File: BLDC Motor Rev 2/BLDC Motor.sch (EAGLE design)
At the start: 51 parts, among them IC1 7805TV, IC2 7815TV, Q1 TP2104, Q10 TP2104, Q12 IRFS, Q13 TP2104, Q15 IRFS, Q16 TP2104, Q18 IRFS, Q3 IRFS, Q4 TP2104, Q6 IRFS, Q7 TP2104, Q9 IRFS, U1 ATMEGA328P_TQFP, Y1 16M

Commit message: Updated BLDC schematic
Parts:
- added R15: 100k, SparkFun:RESISTOR0805-RES
- added R16: 20k, SparkFun:RESISTOR0805-RES
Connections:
- removed net N$12: U1.ADC7
- new net BATTLEVEL: R15.1, R16.2, U1.ADC7
- net BATTPOS: now also R15.2
- net GND: now also R16.1
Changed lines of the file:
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@@
 <grid distance="0.1" unitdist="inch" unit="inch" style="lines" multiple="1" display="no" altdistance="0.01" altunitdist="inch" altunit="inch"/>
 <layers>
-<layer number="1" name="Top" color="4" fill="1" visible="yes" active="no"/>
-<layer number="16" name="Bottom" color="1" fill="1" visible="yes" active="no"/>
-<layer number="17" name="Pads" color="2" fill="1" visible="yes" active="no"/>
-<layer number="18" name="Vias" color="2" fill="1" visible="yes" active="no"/>
-<layer number="19" name="Unrouted" color="6" fill="1" visible="yes" active="no"/>
-<layer number="20" name="Dimension" color="15" fill="1" visible="yes" active="no"/>
-<layer number="21" name="tPlace" color="7" fill="1" visible="yes" active="no"/>
-<layer number="22" name="bPlace" color="7" fill="1" visible="yes" active="no"/>
-<layer number="23" name="tOrigins" color="15" fill="1" visible="yes" active="no"/>
-<layer number="24" name="bOrigins" color="15" fill="1" visible="yes" active="no"/>
-<layer number="25" name="tNames" color="7" fill="1" visible="yes" active="no"/>
-<layer number="26" name="bNames" color="7" fill="1" visible="yes" active="no"/>
-<layer number="27" name="tValues" color="7" fill="1" visible="yes" active="no"/>
-<layer number="28" name="bValues" color="7" fill="1" visible="yes" active="no"/>
+<layer number="1" name="Top" color="4" fill="1" visible="no" active="no"/>
+<layer number="16" name="Bottom" color="1" fill="1" visible="no" active="no"/>
+<layer number="17" name="Pads" color="2" fill="1" visible="no" active="no"/>
+<layer number="18" name="Vias" color="2" fill="1" visible="no" active="no"/>
+<layer number="19" name="Unrouted" color="6" fill="1" visible="no" active="no"/>
+<layer number="20" name="Dimension" color="15" fill="1" visible="no" active="no"/>
+<layer number="21" name="tPlace" color="7" fill="1" visible="no" active="no"/>
+<layer number="22" name="bPlace" color="7" fill="1" visible="no" active="no"/>
+<layer number="23" name="tOrigins" color="15" fill="1" visible="no" active="no"/>
+<layer number="24" name="bOrigins" color="15" fill="1" visible="no" active="no"/>
+<layer number="25" name="tNames" color="7" fill="1" visible="no" active="no"/>
+<layer number="26" name="bNames" color="7" fill="1" visible="no" active="no"/>
+<layer number="27" name="tValues" color="7" fill="1" visible="no" active="no"/>
+<layer number="28" name="bValues" color="7" fill="1" visible="no" active="no"/>
 <layer number="29" name="tStop" color="7" fill="3" visible="no" active="no"/>
 <layer number="30" name="bStop" color="7" fill="6" visible="no" active="no"/>
@@
 <layer number="35" name="tGlue" color="7" fill="4" visible="no" active="no"/>
 <layer number="36" name="bGlue" color="7" fill="5" visible="no" active="no"/>
-<layer number="37" name="tTest" color="7" fill="1" visible="yes" active="no"/>
-<layer number="38" name="bTest" color="7" fill="1" visible="yes" active="no"/>
+<layer number="37" name="tTest" color="7" fill="1" visible="no" active="no"/>
+<layer number="38" name="bTest" color="7" fill="1" visible="no" active="no"/>
 <layer number="39" name="tKeepout" color="4" fill="11" visible="no" active="no"/>
 <layer number="40" name="bKeepout" color="1" fill="11" visible="no" active="no"/>
@@
 <layer number="44" name="Drills" color="7" fill="1" visible="no" active="no"/>
 <layer number="45" name="Holes" color="7" fill="1" visible="no" active="no"/>
-<layer number="46" name="Milling" color="3" fill="1" visible="yes" active="no"/>
-<layer number="47" name="Measures" color="7" fill="1" visible="yes" active="no"/>
-<layer number="48" name="Document" color="7" fill="1" visible="yes" active="no"/>
-<layer number="49" name="Reference" color="7" fill="1" visible="yes" active="no"/>
-<layer number="50" name="dxf" color="7" fill="1" visible="yes" active="no"/>
-<layer number="51" name="tDocu" color="7" fill="1" visible="yes" active="no"/>
-<layer number="52" name="bDocu" color="7" fill="1" visible="yes" active="no"/>
-<layer number="53" name="tGND_GNDA" color="7" fill="9" visible="yes" active="no"/>
-<layer number="54" name="bGND_GNDA" color="1" fill="9" visible="yes" active="no"/>
-<layer number="56" name="wert" color="7" fill="1" visible="yes" active="no"/>
-<layer number="57" name="tCAD" color="7" fill="1" visible="yes" active="no"/>
-<layer number="59" name="tCarbon" color="7" fill="1" visible="yes" active="no"/>
-<layer number="60" name="bCarbon" color="7" fill="1" visible="yes" active="no"/>
+<layer number="46" name="Milling" color="3" fill="1" visible="no" active="no"/>
+<layer number="47" name="Measures" color="7" fill="1" visible="no" active="no"/>
+<layer number="48" name="Document" color="7" fill="1" visible="no" active="no"/>
+<layer number="49" name="Reference" color="7" fill="1" visible="no" active="no"/>
+<layer number="50" name="dxf" color="7" fill="1" visible="no" active="no"/>
+<layer number="51" name="tDocu" color="7" fill="1" visible="no" active="no"/>
+<layer number="52" name="bDocu" color="7" fill="1" visible="no" active="no"/>
+<layer number="53" name="tGND_GNDA" color="7" fill="9" visible="no" active="no"/>
+<layer number="54" name="bGND_GNDA" color="1" fill="9" visible="no" active="no"/>
+<layer number="56" name="wert" color="7" fill="1" visible="no" active="no"/>
+<layer number="57" name="tCAD" color="7" fill="1" visible="no" active="no"/>
+<layer number="59" name="tCarbon" color="7" fill="1" visible="no" active="no"/>
+<layer number="60" name="bCarbon" color="7" fill="1" visible="no" active="no"/>
 <layer number="90" name="Modules" color="5" fill="1" visible="yes" active="yes"/>
 <layer number="91" name="Nets" color="2" fill="1" visible="yes" active="yes"/>
@@
 <part name="Q15" library="D2PAK-7" deviceset="NMOSFET-D2PAK-7" device="" value="IRFS"/>
 <part name="Q18" library="D2PAK-7" deviceset="NMOSFET-D2PAK-7" device="" value="IRFS"/>
+<part name="R15" library="SparkFun" deviceset="RESISTOR" device="0805-RES" value="100k"/>
+<part name="R16" library="SparkFun" deviceset="RESISTOR" device="0805-RES" value="20k"/>
 </parts>
 <sheets>
@@
 <instance part="Q15" gate="G$1" x="223.52" y="96.52"/>
 <instance part="Q18" gate="G$1" x="172.72" y="96.52"/>
+<instance part="R15" gate="G$1" x="187.96" y="238.76" rot="R90"/>
+<instance part="R16" gate="G$1" x="187.96" y="218.44" rot="R90"/>
 </instances>
 <busses>
@@
 <segment>
 <pinref part="IC1" gate="A1" pin="GND"/>
-<wire x1="208.28" y1="213.36" x2="208.28" y2="210.82" width="0.1524" layer="91"/>
 <pinref part="GND6" gate="1" pin="GND"/>
+<pinref part="R16" gate="G$1" pin="1"/>
+<wire x1="187.96" y1="213.36" x2="187.96" y2="210.82" width="0.1524" layer="91"/>
+<wire x1="187.96" y1="210.82" x2="208.28" y2="210.82" width="0.1524" layer="91"/>
+<wire x1="208.28" y1="210.82" x2="208.28" y2="213.36" width="0.1524" layer="91"/>
 </segment>
 <segment>
@@
 </segment>
 </net>
-<net name="N$12" class="0">
-<segment>
-<pinref part="U1" gate="U$1" pin="ADC7"/>
-<wire x1="101.6" y1="190.5" x2="106.68" y2="190.5" width="0.1524" layer="91"/>
-</segment>
-</net>
 <net name="N$15" class="0">
 <segment>
@@
 <wire x1="198.12" y1="243.84" x2="187.96" y2="243.84" width="0.1524" layer="91"/>
 <label x="187.96" y="243.84" size="1.778" layer="95"/>
+<pinref part="R15" gate="G$1" pin="2"/>
 </segment>
 <segment>
@@
 </segment>
 </net>
+<net name="BATTLEVEL" class="0">
+<segment>
+<pinref part="R15" gate="G$1" pin="1"/>
+<pinref part="R16" gate="G$1" pin="2"/>
+<wire x1="187.96" y1="233.68" x2="187.96" y2="223.52" width="0.1524" layer="91"/>
+<wire x1="187.96" y1="223.52" x2="180.34" y2="223.52" width="0.1524" layer="91"/>
+<junction x="187.96" y="223.52"/>
+<label x="180.34" y="223.52" size="1.778" layer="95"/>
+<pinref part="U1" gate="U$1" pin="ADC7"/>
+<wire x1="101.6" y1="190.5" x2="124.46" y2="190.5" width="0.1524" layer="91"/>
+<wire x1="124.46" y1="190.5" x2="124.46" y2="195.58" width="0.1524" layer="91"/>
+<wire x1="124.46" y1="195.58" x2="180.34" y2="195.58" width="0.1524" layer="91"/>
+<wire x1="180.34" y1="195.58" x2="180.34" y2="223.52" width="0.1524" layer="91"/>
+</segment>
+</net>

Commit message: Updating board
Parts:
- removed JP4: STAND-OFF, SparkFun:STAND-OFF
- added JP1: STAND-OFF, SparkFun:STAND-OFF
- R16: value 20k -> 22k
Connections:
- net MOSI: now also Q4.G, Q5.G, R10.2; no longer Q16.G, Q17.G, R14.2
- net PULSE2: now also Q16.G, Q17.G, R14.2; no longer Q4.G, Q5.G, R10.2
- net PULSE3: now also Q13.G, Q14.G, R13.2; no longer Q7.G, Q8.G, R11.2
- net PULSE5: now also Q7.G, Q8.G, R11.2; no longer Q13.G, Q14.G, R13.2

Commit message: Adding capacitors to the processor for better stability
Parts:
- added C4, C6, C7: 22pf, SparkFun:CAP0805
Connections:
- new net N$7: C7.2, U1.AREF
- net GND: now also C4.1, C6.1, C7.1
- net VCC: now also C4.2, C6.2
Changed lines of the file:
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@@
 <part name="JP1" library="SparkFun" deviceset="STAND-OFF" device=""/>
 <part name="JP2" library="SparkFun" deviceset="STAND-OFF" device=""/>
+<part name="C4" library="SparkFun" deviceset="CAP" device="0805" value="22pf"/>
+<part name="C6" library="SparkFun" deviceset="CAP" device="0805" value="22pf"/>
+<part name="C7" library="SparkFun" deviceset="CAP" device="0805" value="22pf"/>
+<part name="GND26" library="SparkFun" deviceset="GND" device=""/>
+<part name="GND27" library="SparkFun" deviceset="GND" device=""/>
+<part name="GND28" library="SparkFun" deviceset="GND" device=""/>
 </parts>
 <sheets>
@@
 <instance part="JP1" gate="G$1" x="15.24" y="223.52"/>
 <instance part="JP2" gate="G$1" x="15.24" y="208.28"/>
+<instance part="C4" gate="G$1" x="43.18" y="203.2" rot="R90"/>
+<instance part="C6" gate="G$1" x="43.18" y="198.12" rot="R90"/>
+<instance part="C7" gate="G$1" x="50.8" y="193.04" rot="R90"/>
+<instance part="GND26" gate="1" x="35.56" y="203.2" rot="R270"/>
+<instance part="GND27" gate="1" x="35.56" y="198.12" rot="R270"/>
+<instance part="GND28" gate="1" x="43.18" y="193.04" rot="R270"/>
 </instances>
 <busses>
@@
 <wire x1="187.96" y1="210.82" x2="208.28" y2="210.82" width="0.1524" layer="91"/>
 <wire x1="208.28" y1="210.82" x2="208.28" y2="213.36" width="0.1524" layer="91"/>
+<junction x="208.28" y="210.82"/>
 </segment>
 <segment>
@@
 <pinref part="R14" gate="G$1" pin="1"/>
 <pinref part="GND25" gate="1" pin="GND"/>
+</segment>
+<segment>
+<pinref part="C4" gate="G$1" pin="1"/>
+<pinref part="GND26" gate="1" pin="GND"/>
+</segment>
+<segment>
+<pinref part="C6" gate="G$1" pin="1"/>
+<pinref part="GND27" gate="1" pin="GND"/>
+</segment>
+<segment>
+<pinref part="C7" gate="G$1" pin="1"/>
+<pinref part="GND28" gate="1" pin="GND"/>
+<junction x="45.72" y="193.04"/>
+<pinref part="GND28" gate="1" pin="GND"/>
 </segment>
 </net>
@@
 <wire x1="50.8" y1="218.44" x2="45.72" y2="218.44" width="0.1524" layer="91"/>
 <junction x="45.72" y="218.44"/>
+<pinref part="C4" gate="G$1" pin="2"/>
+<pinref part="C6" gate="G$1" pin="2"/>
+<junction x="45.72" y="198.12"/>
 </segment>
 <segment>
@@
 </segment>
 </net>
+<net name="N$7" class="0">
+<segment>
+<pinref part="U1" gate="U$1" pin="AREF"/>
+<pinref part="C7" gate="G$1" pin="2"/>
+<junction x="53.34" y="193.04"/>
+</segment>
+</net>

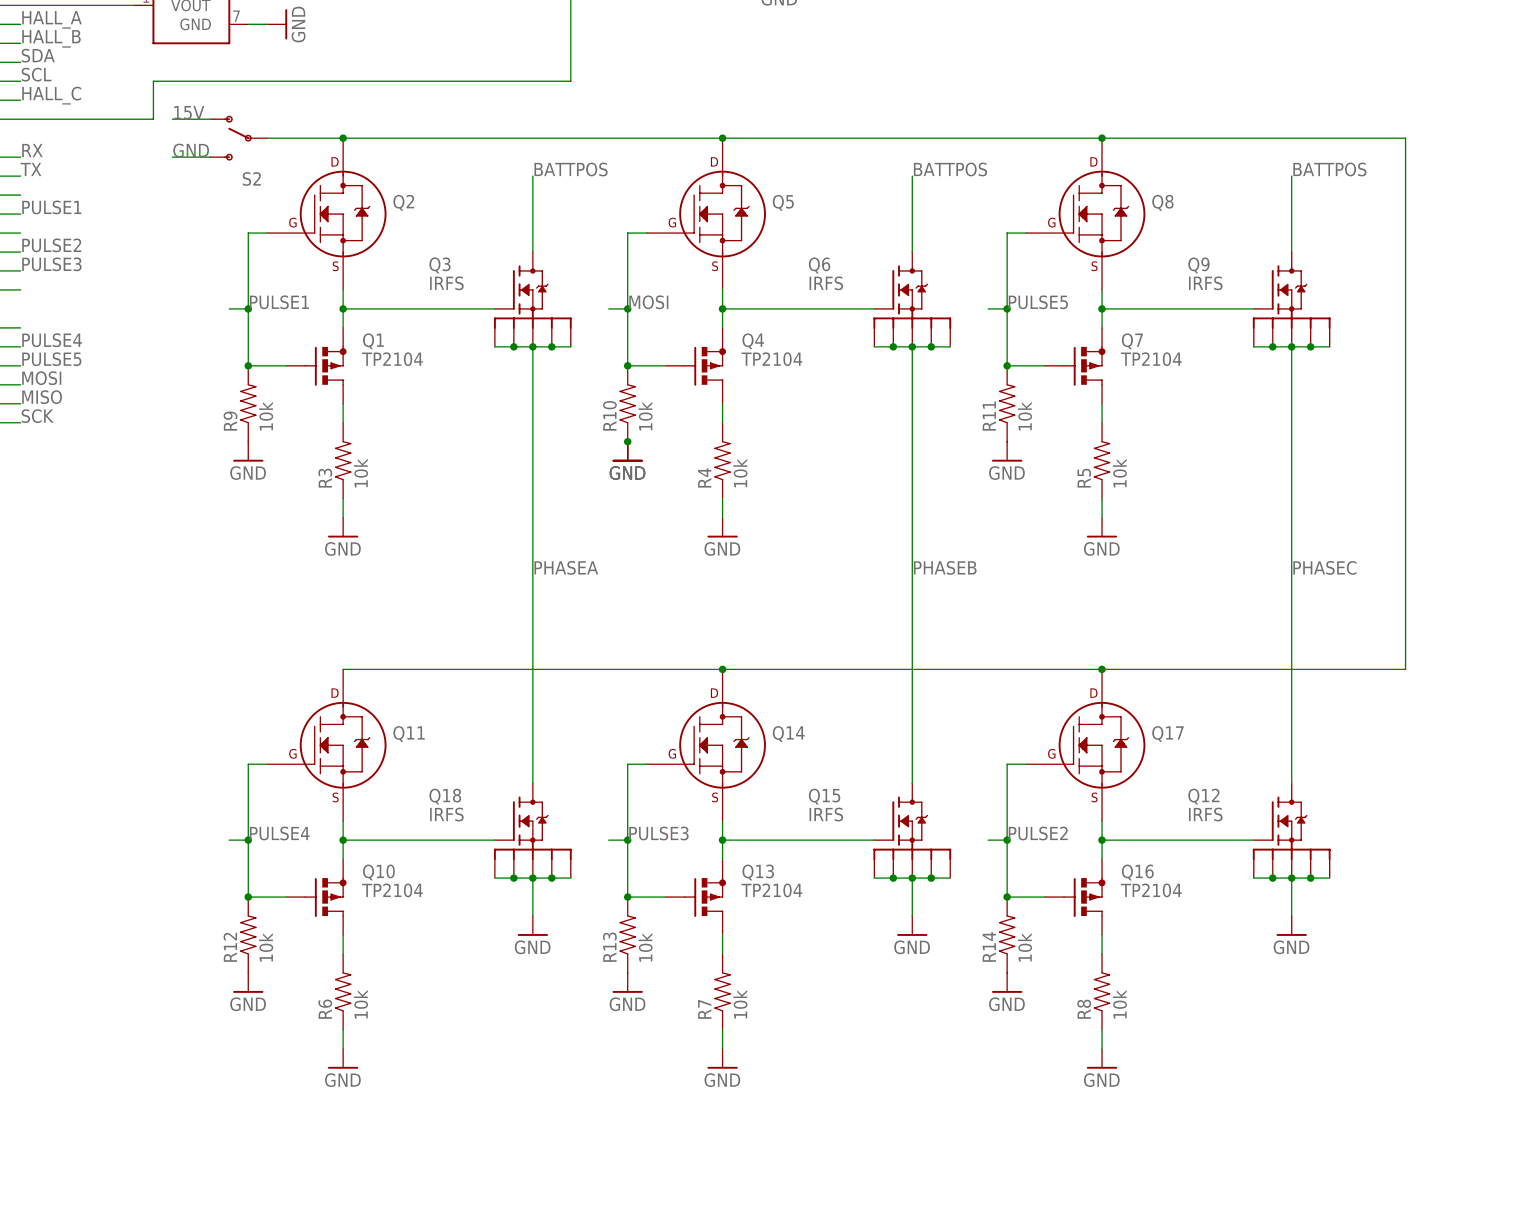
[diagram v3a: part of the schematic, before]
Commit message: Updated Gate driver on board, moved weekly reports to folder
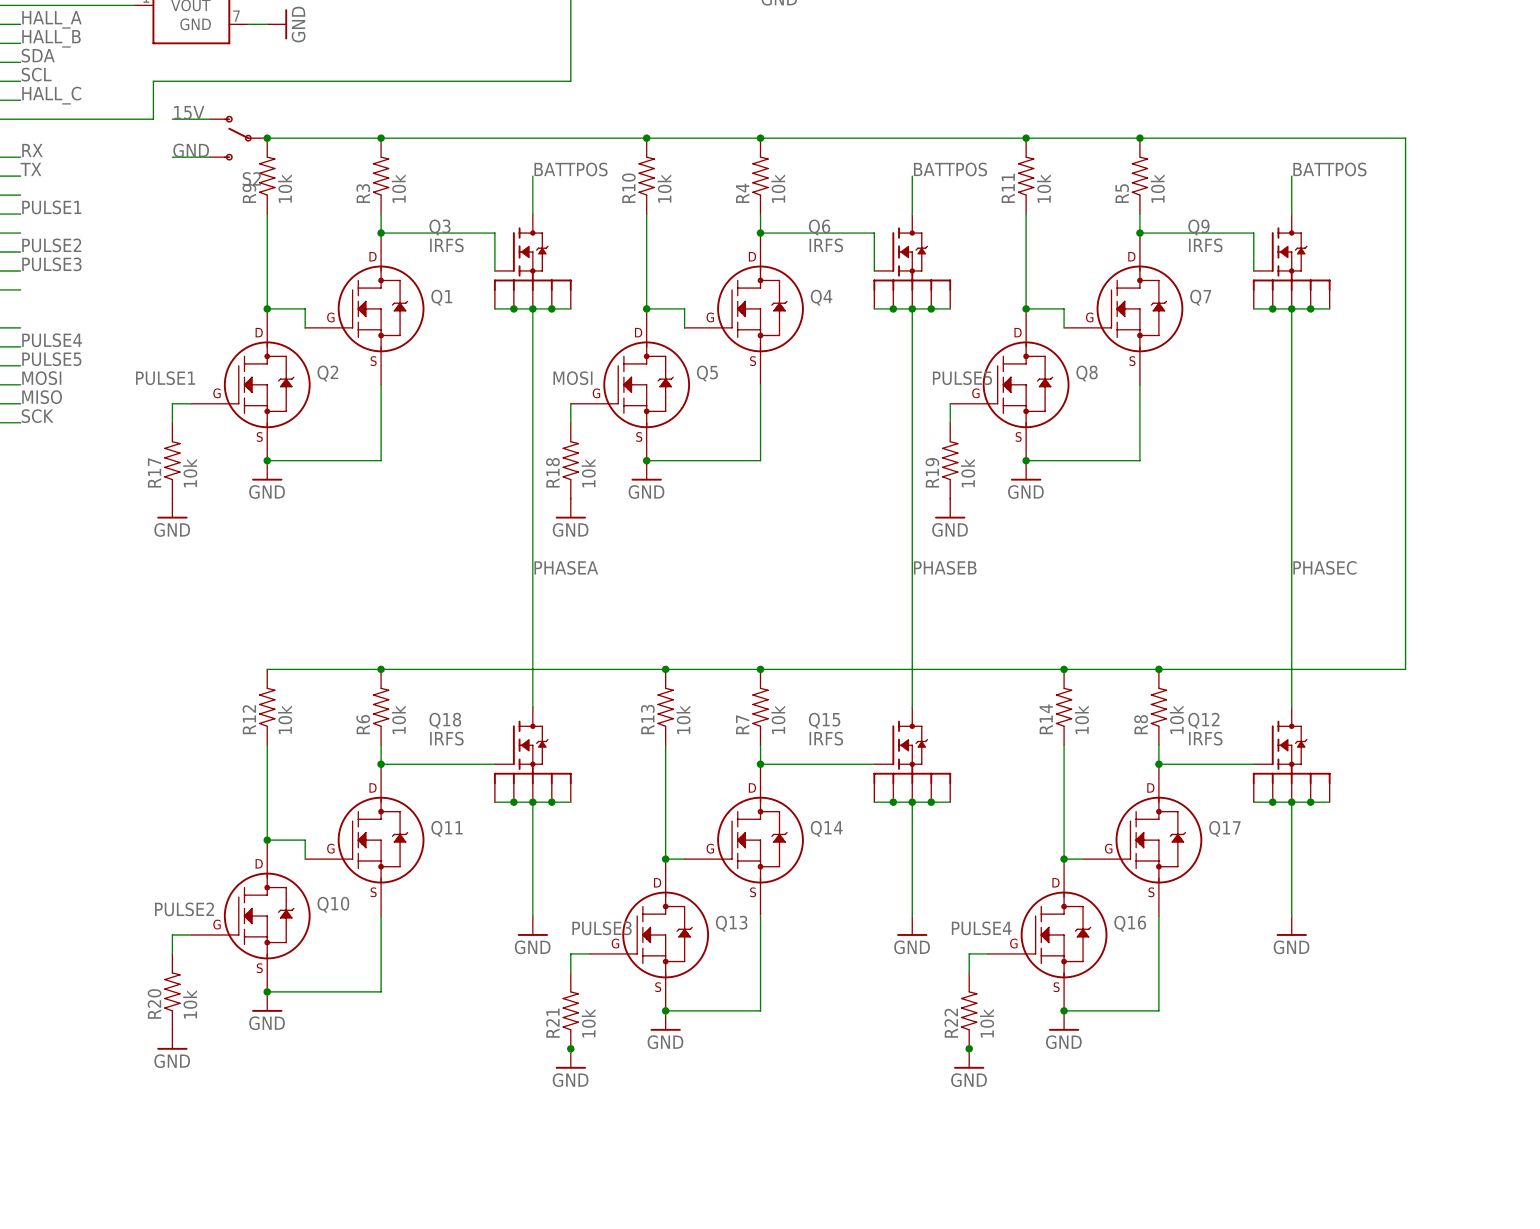
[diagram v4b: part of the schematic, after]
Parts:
- added R17, R18, R19, R20, R21, R22: 10k, SparkFun:RESISTOR0805-RES
- Q1, Q10, Q13, Q16, Q4, Q7: value TP2104 -> (none); device adafruit:PFETTP0610KL -> transistors:2N7000_TO92
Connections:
- removed net N$10: Q4.D, R4.2
- removed net N$16: Q7.S, Q8.S, Q9.G
- removed net N$18: Q10.D, R6.2
- removed net N$23: Q13.S, Q14.S, Q15.G
- removed net N$24: Q16.D, R8.2
- removed net N$25: Q12.G, Q16.S, Q17.S
- new net N$11: Q4.G, Q5.D, R10.1
- new net N$12: R10.2, R11.2, R12.2, R13.2, R14.2, R3.2, R4.2, R5.2, R6.2, R7.2, R8.2, R9.2, S2.P
- new net N$26: Q12.G, Q17.D, R8.1
- new net N$27: Q16.D, Q17.G, R14.1
- new net N$28: Q14.D, Q15.G, R7.1
- new net N$8: Q1.G, Q2.D, R9.1
- net GND: now also Q1.S, Q10.S, Q11.S, Q13.S, Q14.S, Q16.S, Q17.S, Q2.S, Q4.S, Q5.S, Q7.S, Q8.S, R17.1, R18.1, R19.1, R20.1, R21.1, R22.1; no longer R10.1, R11.1, R12.1, R13.1, R14.1, R3.1, R4.1, R5.1, R6.1, R7.1, R8.1, R9.1
- net MOSI: now also R18.2; no longer Q4.G, R10.2
- net N$13: now also Q7.D, Q9.G, R5.1; no longer Q4.S, Q5.S, Q6.G
- net N$14: now also Q7.G, Q8.D, R11.1; no longer Q7.D, R5.2
- net N$19: now also Q11.D, R6.1; no longer Q10.S, Q11.S
- net N$22: now also Q14.G, R13.1; no longer R7.2
- net N$4: now also Q10.D, Q11.G, R12.1; no longer Q1.D, R3.2
- net N$5: now also Q1.D, R3.1; no longer Q1.S, Q2.S
- net N$9: now also Q4.D, Q6.G, R4.1; no longer Q11.D, Q14.D, Q17.D, Q2.D, Q5.D, Q8.D, S2.P
- net PULSE1: now also R17.2; no longer Q1.G, R9.2
- net PULSE2: now also Q10.G, R20.2; no longer Q16.G, Q17.G, R14.2
- net PULSE3: now also R21.2; no longer Q14.G, R13.2
- net PULSE4: now also Q16.G, R22.2; no longer Q10.G, Q11.G, R12.2
- net PULSE5: now also R19.2; no longer Q7.G, R11.2
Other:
- moved on the sheet: Q11, Q12, Q14, Q15, Q17, Q18, Q2, Q3, Q5, Q6, Q8, Q9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
